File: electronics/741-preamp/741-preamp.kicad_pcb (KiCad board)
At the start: 2 copper layers, 13 parts, among them J1 PWR, J2 Audio In, J3 OUT, U1 LM741

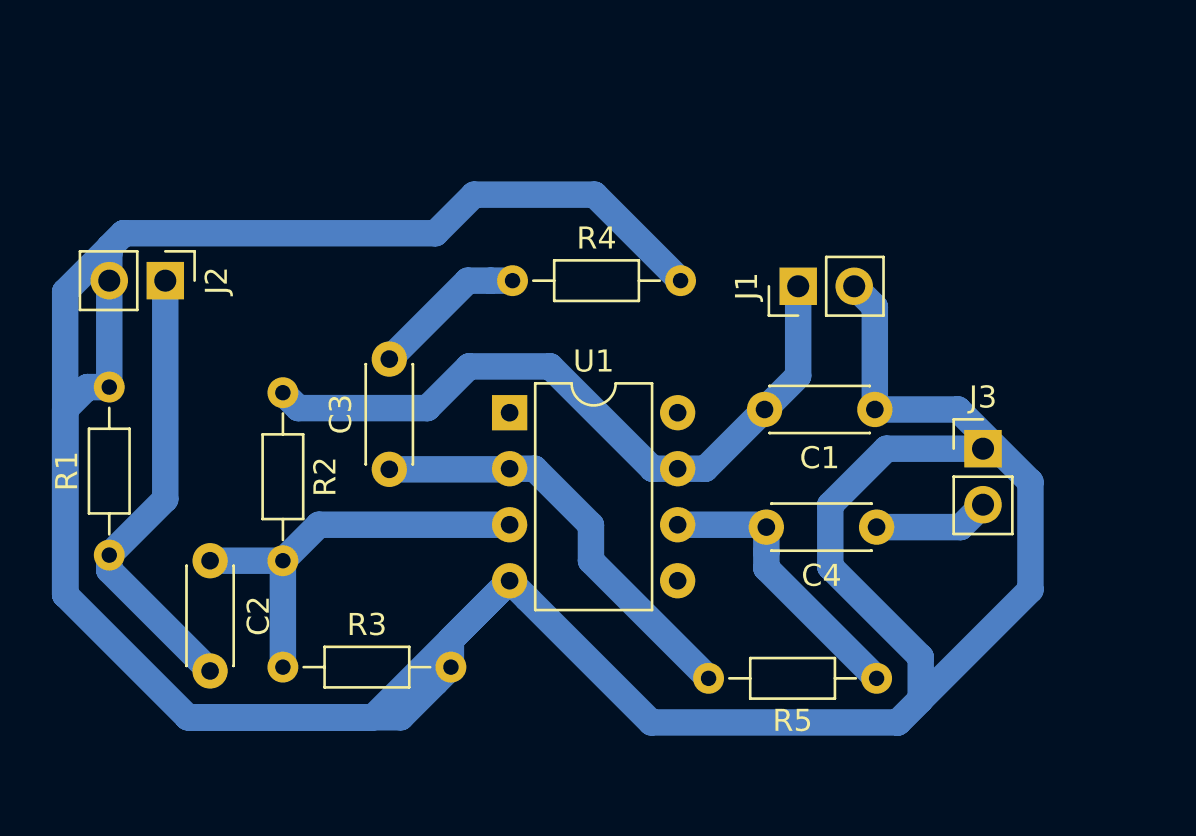
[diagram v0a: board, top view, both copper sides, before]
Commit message: PCB with connectors
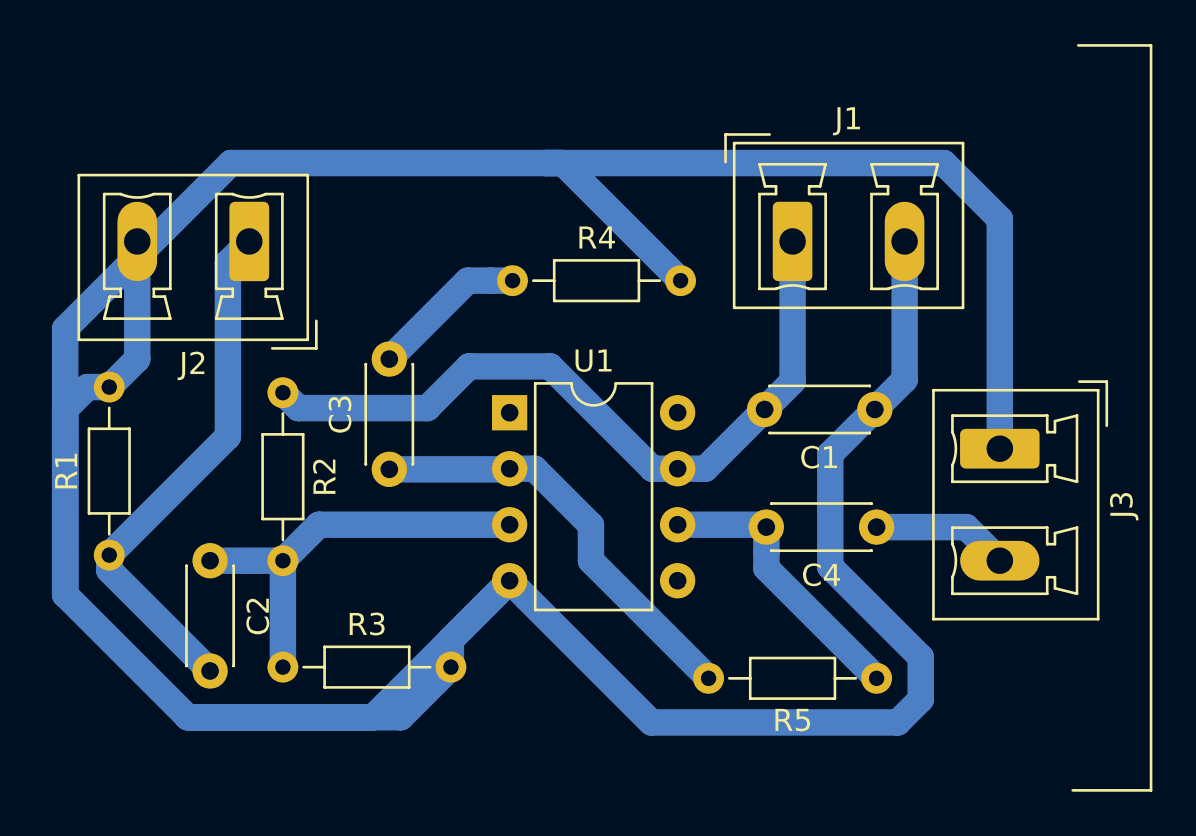
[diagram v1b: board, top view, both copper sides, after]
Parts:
- J1, J2, J3: footprint Connector_PinHeader_2.54mm:PinHeader_1x02_P2.54mm_Vertical -> Connector_Phoenix_MC_HighVoltage:PhoenixContact_MCV_1,5_2-G-5.08_1x02_P5.08mm_Vertical
- moved J2 4.20 mm to (89.7, 37.1), turned to 180 degrees
- moved J1 2.05 mm to (114.3, 37.1), turned to 0 degrees
- moved J3 0.76 mm to (123.7, 46.5), turned to 270 degrees
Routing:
- net GND: track 174.1 -> 182.3 mm
- net Net-(C2-Pad2): track 20.6 -> 24.0 mm
- net Net-(C4-Pad1): track 5.25 -> 6.22 mm
